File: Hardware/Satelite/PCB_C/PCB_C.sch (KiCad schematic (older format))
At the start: 49 parts, among them IC1 MCP1501T-33E_CHY, J1 SWD, J3 Conector_PCB_B-C, J4 Conector_Expansion_CanSat, J5 USB_B_Micro, M1 Spacer, M2 Spacer, M3 Spacer, U1 TXS0104ERGYR, U2 TCA9802DGKR, U3 W25Q32JVSSIQ, U4 TXS0104ERGYR, U5 BL654, Y1 LFXTAL016178

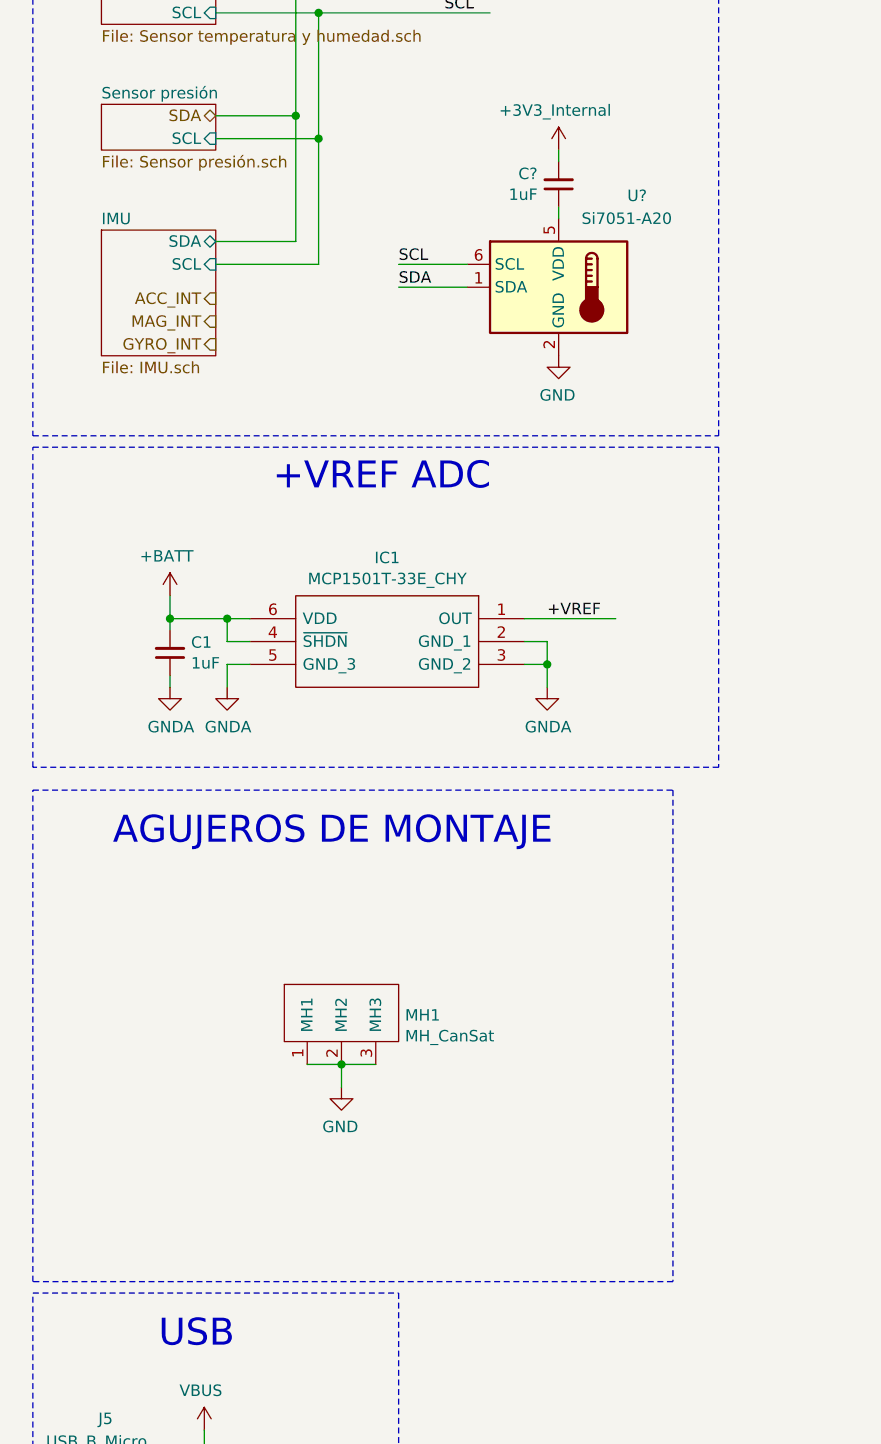
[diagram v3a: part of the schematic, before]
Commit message: Eliminada referencia de tensión no usada en PCB_C
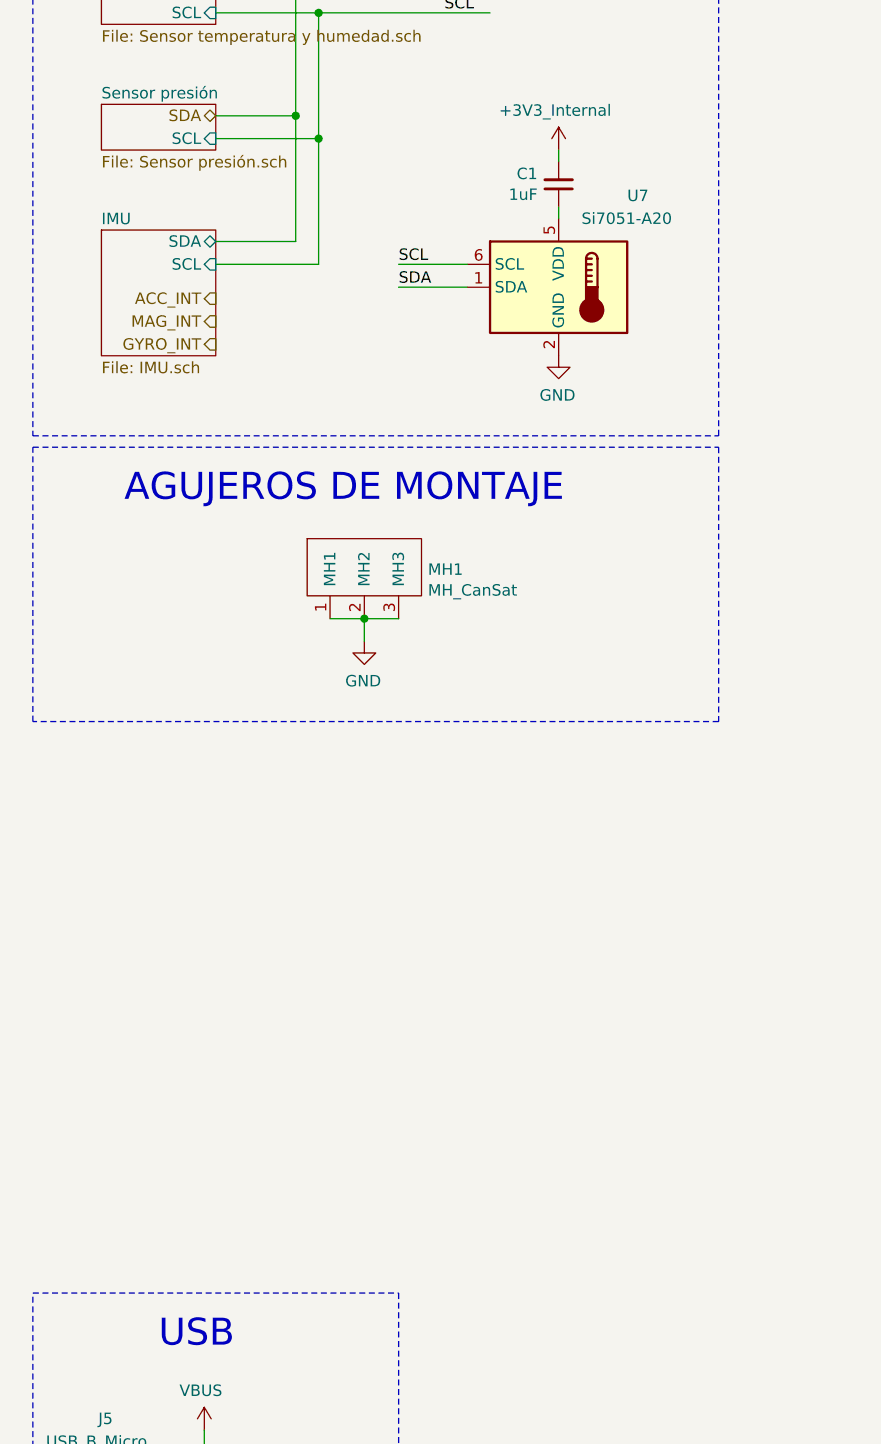
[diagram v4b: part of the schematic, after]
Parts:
- removed C1: 1uF, Capacitor_SMD:C_0402_1005Metric, symbol Device:C_Small
- removed IC1: MCP1501T-33E_CHY, SamacSys_Parts:SOT95P270X145-6N, symbol SamacSys_Parts:MCP1501T-33E_CHY
- gave numbers to parts that had none: 2
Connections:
- net labels removed: GNDA
- wire segments 313 -> 299
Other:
- note removed: "+VREF ADC"
- moved on the sheet: MH1
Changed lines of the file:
@@
-$Comp
-L Device:C_Small C?
-U 1 1 5BCA2C7F
-P 1150 4000
-AR Path="/5BB122CA/5BCA2C7F" Ref="C?"  Part="1"
-AR Path="/5BB12371/5BCA2C7F" Ref="C?"  Part="1"
-AR Path="/5BCA2C7F" Ref="C1"  Part="1"
-F 0 "C1" H 1058 3954 50  0000 R CNN
-F 1 "1uF" H 1058 4045 50  0000 R CNN
-F 2 "Capacitor_SMD:C_0402_1005Metric" H 1150 4000 50  0001 C CNN
-F 3 "~" H 1150 4000 50  0001 C CNN
-F 4 "GRM155R61E105KA12D" H 1150 4000 50  0001 C CNN "Manufacturer Part Number"
-	1    1150 4000
-	-1   0    0    1
-$EndComp
 $Comp
 L Device:C_Small C?
@@
 Text Label 10250 5050 2    50   ~ 0
 SPI_BUFFER_EN
-Text Notes 1600 3300 0    118  ~ 0
-+VREF ADC
-Wire Notes Line
-	550  4500 550  3100
-Wire Notes Line
-	3550 4500 550  4500
-Wire Notes Line
-	3550 3100 3550 4500
-Wire Notes Line
-	550  3100 3550 3100
-Wire Wire Line
-	2700 3850 3100 3850
-Text Label 2800 3850 0    50   ~ 0
-+VREF
-Wire Wire Line
-	2800 4050 2800 4150
-Wire Wire Line
-	2700 4050 2800 4050
-Wire Wire Line
-	2800 3950 2700 3950
-Connection ~ 2800 4050
-Wire Wire Line
-	2800 3950 2800 4050
-Wire Wire Line
-	1400 4050 1400 4150
-Wire Wire Line
-	1500 4050 1400 4050
-Wire Wire Line
-	1400 3850 1150 3850
-Wire Wire Line
-	1400 3950 1400 3850
-Wire Wire Line
-	1500 3950 1400 3950
-Connection ~ 1400 3850
-Wire Wire Line
-	1500 3850 1400 3850
-Wire Wire Line
-	1150 4100 1150 4150
-Wire Wire Line
-	1150 3900 1150 3850
-Connection ~ 1150 3850
-Wire Wire Line
-	1150 3850 1150 3750
-$Comp
-L SamacSys_Parts:MCP1501T-33E_CHY IC1
-U 1 1 5BC3E089
-P 2700 3850
-F 0 "IC1" H 3300 4116 50  0000 C CNN
-F 1 "MCP1501T-33E_CHY" H 3300 4024 50  0000 C CNN
-F 2 "SamacSys_Parts:SOT95P270X145-6N" H 3750 3950 50  0001 L CNN
-F 3 "https://componentsearchengine.com/Datasheets/1/MCP1501T-33E_CHY.pdf" H 3750 3850 50  0001 L CNN
-F 4 "Voltage References Precision Buffered Voltage Reference" H 3750 3750 50  0001 L CNN "Description"
-F 5 "1.45" H 3750 3650 50  0001 L CNN "Height"
-F 6 "Microchip" H 3750 3550 50  0001 L CNN "Manufacturer_Name"
-F 7 "MCP1501T-33E/CHY" H 3750 3450 50  0001 L CNN "Manufacturer Part Number"
-F 8 "MCP1501T-33E/CHY" H 3750 3150 50  0001 L CNN "Arrow Part Number"
-F 9 "https://www.arrow.com/en/products/mcp1501t-33echy/microchip-technology" H 3750 3050 50  0001 L CNN "Arrow Price/Stock"
-	1    2700 3850
-	-1   0    0    -1
-$EndComp
 $Comp
 L AXTEC_IC:Conector_Expansion_CanSat J4
@@
 Wire Wire Line
 	15100 4650 15550 4650
-$Comp
-L power:+BATT #PWR01
-U 1 1 5BC3E6F0
-P 1150 3750
-F 0 "#PWR01" H 1150 3600 50  0001 C CNN
-F 1 "+BATT" H 1165 3923 50  0000 C CNN
-F 2 "" H 1150 3750 50  0001 C CNN
-F 3 "" H 1150 3750 50  0001 C CNN
-	1    1150 3750
-	-1   0    0    -1
-$EndComp
 $Comp
 L Graphic:Logo_Open_Hardware_Large #LOGO1
@@
 Wire Wire Line
 	13500 8750 13850 8750
-$Comp
-L power:GNDA #PWR0103
-U 1 1 5C301DAD
-P 2800 4150
-F 0 "#PWR0103" H 2800 3900 50  0001 C CNN
-F 1 "GNDA" H 2804 3976 50  0000 C CNN
-F 2 "" H 2800 4150 50  0001 C CNN
-F 3 "" H 2800 4150 50  0001 C CNN
-	1    2800 4150
-	1    0    0    -1
-$EndComp
-$Comp
-L power:GNDA #PWR0106
-U 1 1 5C375184
-P 1400 4150
-F 0 "#PWR0106" H 1400 3900 50  0001 C CNN
-F 1 "GNDA" H 1404 3976 50  0000 C CNN
-F 2 "" H 1400 4150 50  0001 C CNN
-F 3 "" H 1400 4150 50  0001 C CNN
-	1    1400 4150
-	1    0    0    -1
-$EndComp
-$Comp
-L power:GNDA #PWR0107
-U 1 1 5C375315
-P 1150 4150
-F 0 "#PWR0107" H 1150 3900 50  0001 C CNN
-F 1 "GNDA" H 1154 3976 50  0000 C CNN
-F 2 "" H 1150 4150 50  0001 C CNN
-F 3 "" H 1150 4150 50  0001 C CNN
-	1    1150 4150
-	1    0    0    -1
-$EndComp
 $Bitmap
 Pos 12950 10250
@@
 	2600 11150 5650 11150
 Wire Notes Line
-	550  6750 550  4600
+	550  4300 550  3100
 Wire Notes Line
-	3350 6750 550  6750
-Wire Notes Line
-	3350 4600 3350 6750
-Wire Notes Line
-	550  4600 3350 4600
+	550  3100 3550 3100
 $Comp
 L Device:R R6
@@
 	1    0    0    -1
 $EndComp
-$Comp
-L AXTEC_IC:MH_CanSat MH1
-U 1 1 5BCAAD71
-P 1900 5700
-F 0 "MH1" H 2178 5815 50  0000 L CNN
-F 1 "MH_CanSat" H 2178 5724 50  0000 L CNN
-F 2 "AXTEC:MH_CanSat" H 1900 5700 50  0001 C CNN
-F 3 "" H 1900 5700 50  0001 C CNN
-	1    1900 5700
-	1    0    0    -1
-$EndComp
-$Comp
-L power:GND #PWR081
-U 1 1 5BCAAE9A
-P 1900 5900
-F 0 "#PWR081" H 1900 5650 50  0001 C CNN
-F 1 "GND" H 1905 5727 50  0000 C CNN
-F 2 "" H 1900 5900 50  0001 C CNN
-F 3 "" H 1900 5900 50  0001 C CNN
-	1    1900 5900
-	-1   0    0    -1
-$EndComp
-Wire Wire Line
-	1750 5800 1900 5800
-Connection ~ 1900 5800
-Wire Wire Line
-	1900 5800 2050 5800
-Wire Wire Line
-	1900 5900 1900 5800
-Text Notes 900  4850 0    118  ~ 0
+Text Notes 950  3350 0    118  ~ 0
 AGUJEROS DE MONTAJE
 Wire Wire Line
@@
 nRST
 $Comp
-L Sensor_Temperature:Si7051-A20 U?
+L Sensor_Temperature:Si7051-A20 U7
 U 1 1 5D3B31C1
 P 2850 2400
-F 0 "U?" H 3150 2800 50  0000 L CNN
+F 0 "U7" H 3150 2800 50  0000 L CNN
 F 1 "Si7051-A20" H 2950 2700 50  0000 L CNN
 F 2 "Package_DFN_QFN:DFN-6-1EP_3x3mm_P1mm_EP1.65x2.55mm" H 2850 2000 50  0001 C CNN
@@
 $EndComp
 $Comp
-L AXTEC_IC:+3V3_Internal #PWR?
+L AXTEC_IC:+3V3_Internal #PWR1
 U 1 1 5D3FBC3E
 P 2850 1800
-F 0 "#PWR?" H 2850 2200 50  0001 C CNN
+F 0 "#PWR1" H 2850 2200 50  0001 C CNN
 F 1 "+3V3_Internal" H 2835 1973 50  0000 C CNN
 F 2 "" H 2850 1800 50  0001 C CNN
@@
 AR Path="/5BB122CA/5D3FD0BC" Ref="C?"  Part="1"
 AR Path="/5BB12371/5D3FD0BC" Ref="C?"  Part="1"
-F 0 "C?" H 2758 1904 50  0000 R CNN
+AR Path="/5D3FD0BC" Ref="C1"  Part="1"
+F 0 "C1" H 2758 1904 50  0000 R CNN
 F 1 "1uF" H 2758 1995 50  0000 R CNN
 F 2 "Capacitor_SMD:C_0402_1005Metric" H 2850 1950 50  0001 C CNN
@@
 	2850 2050 2850 2100
 $Comp
-L power:GND #PWR?
+L power:GND #PWR041
 U 1 1 5D45F3A9
 P 2850 2700
-F 0 "#PWR?" H 2850 2450 50  0001 C CNN
+F 0 "#PWR041" H 2850 2450 50  0001 C CNN
 F 1 "GND" H 2855 2527 50  0000 C CNN
 F 2 "" H 2850 2700 50  0001 C CNN
@@
 Text Label 2150 2300 0    50   ~ 0
 SCL
+Wire Notes Line
+	3550 3100 3550 4300
+Wire Notes Line
+	3550 4300 550  4300
+Wire Wire Line
+	2000 3950 2000 3850
+Wire Wire Line
+	2000 3850 2150 3850
+Connection ~ 2000 3850
+Wire Wire Line
+	1850 3850 2000 3850
+$Comp
+L power:GND #PWR081
+U 1 1 5BCAAE9A
+P 2000 3950
+F 0 "#PWR081" H 2000 3700 50  0001 C CNN
+F 1 "GND" H 2005 3777 50  0000 C CNN
+F 2 "" H 2000 3950 50  0001 C CNN
+F 3 "" H 2000 3950 50  0001 C CNN
+	1    2000 3950
+	-1   0    0    -1
+$EndComp
+$Comp
+L AXTEC_IC:MH_CanSat MH1
+U 1 1 5BCAAD71
+P 2000 3750
+F 0 "MH1" H 2278 3865 50  0000 L CNN
+F 1 "MH_CanSat" H 2278 3774 50  0000 L CNN
+F 2 "AXTEC:MH_CanSat" H 2000 3750 50  0001 C CNN
+F 3 "" H 2000 3750 50  0001 C CNN
+	1    2000 3750
+	1    0    0    -1
+$EndComp
 $EndSCHEMATC

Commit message: Agregado footprints faltantes en PCB_C
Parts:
- U1, U4: footprint RGY(S-PVQFN-N14) -> Package_DFN_QFN:Texas_S-PVQFN-N14
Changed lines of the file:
@@
 F 0 "U4" H 10150 10365 50  0000 C CNN
 F 1 "TXS0104ERGYR" H 10150 10274 50  0000 C CNN
-F 2 "RGY(S-PVQFN-N14)" H 10750 10200 50  0001 L CNN
+F 2 "Package_DFN_QFN:Texas_S-PVQFN-N14" H 10750 10200 50  0001 L CNN
 F 3 "http://www.ti.com/general/docs/lit/getliterature.tsp?genericPartNumber=TXS0104E&&fileType=pdf" H 10750 10100 50  0001 L CNN
 F 4 "Texas Instruments TXS0104ERGYR, Voltage Level Translator, Open Drain, 1.65  3.6 V, 2.3  5.5 V, 14-Pin" H 10750 10000 50  0001 L CNN "Description"
@@
 F 0 "U1" H 4100 10365 50  0000 C CNN
 F 1 "TXS0104ERGYR" H 4100 10274 50  0000 C CNN
-F 2 "RGY(S-PVQFN-N14)" H 4700 10200 50  0001 L CNN
+F 2 "Package_DFN_QFN:Texas_S-PVQFN-N14" H 4700 10200 50  0001 L CNN
 F 3 "http://www.ti.com/general/docs/lit/getliterature.tsp?genericPartNumber=TXS0104E&&fileType=pdf" H 4700 10100 50  0001 L CNN
 F 4 "Texas Instruments TXS0104ERGYR, Voltage Level Translator, Open Drain, 1.65  3.6 V, 2.3  5.5 V, 14-Pin" H 4700 10000 50  0001 L CNN "Description"

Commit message: Agregados footprints faltantes en samacsys + asignacion en PCB_C
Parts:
- U7: footprint Package_DFN_QFN:DFN-6-1EP_3x3mm_P1mm_EP1.65x2.55mm -> Package_DFN_QFN:DFN-6-1EP_3x3mm_P1mm_EP1.5x2.4mm
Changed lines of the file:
@@
 F 0 "U7" H 3150 2800 50  0000 L CNN
 F 1 "Si7051-A20" H 2950 2700 50  0000 L CNN
-F 2 "Package_DFN_QFN:DFN-6-1EP_3x3mm_P1mm_EP1.65x2.55mm" H 2850 2000 50  0001 C CNN
+F 2 "Package_DFN_QFN:DFN-6-1EP_3x3mm_P1mm_EP1.5x2.4mm" H 2850 2000 50  0001 C CNN
 F 3 "https://www.silabs.com/documents/public/data-sheets/Si7050-1-3-4-5-A20.pdf" H 2650 2700 50  0001 C CNN
 F 4 "SI7051-A20-IM" H 2850 2400 50  0001 C CNN "Manufacturer Part Number"

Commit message: PCB_C V2 terminado
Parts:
- removed TP15: TestPoint_RXDBG, TestPoint:TestPoint_Pad_D1.0mm, symbol Connector:TestPoint_Probe
- TP1, TP10, TP11, TP2, TP3, TP4, TP7, TP8, TP9: footprint TestPoint:TestPoint_Pad_D1.0mm -> TestPoint:TestPoint_Pad_D1.5mm
- TP12: value TestPoint_SCLPIC -> TestPoint_SD0; footprint TestPoint:TestPoint_Pad_D1.0mm -> TestPoint:TestPoint_Pad_D1.5mm
- TP13: value TestPoint_SDAPIC -> TestPoint_SCLK; footprint TestPoint:TestPoint_Pad_D1.0mm -> TestPoint:TestPoint_Pad_D1.5mm
- TP14: value TestPoint_TXDBG -> TestPoint_CS; footprint TestPoint:TestPoint_Pad_D1.0mm -> TestPoint:TestPoint_Pad_D1.5mm
- TP5: footprint TestPoint:TestPoint_THTPad_1.0x1.0mm_Drill0.5mm -> TestPoint:TestPoint_THTPad_1.5x1.5mm_Drill0.7mm
- TP6: value TestPoint_VREF -> TestPoint_SDI; footprint TestPoint:TestPoint_Pad_D1.0mm -> TestPoint:TestPoint_Pad_D1.5mm
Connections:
- net labels added: ENABLE_3V3, ENABLE_5V
- net labels removed: +VREF, AUX_ENABLE, CHG_DETECT, RX_DEBUG, SCL_PIC16, SDA_PIC16, TX_DEBUG
- wire segments 299 -> 316
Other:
- moved on the sheet: C1, C6, R1, R4

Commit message: Conectores con más altura y nuevos separadores en PCB_C
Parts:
- J3: Manufacturer Part Number 53307-2071 -> 53353-1071; Notes Hecho con dos 53307-2071 y sus dos opuestos 52465-2071 -> Hecho con dos 53353-1071 y sus dos opuestos 52465-2071
- M1, M2, M3: Manufacturer Part Number R30-3011002 -> R30-3010702
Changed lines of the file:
@@
 F 2 "AXTEC:Conector_PCB_B-C_Lado_C" H 14150 2200 50  0001 C CNN
 F 3 "" H 14150 2200 50  0001 C CNN
-F 4 "Hecho con dos 53307-2071 y sus dos opuestos 52465-2071" H 0   -150 50  0001 C CNN "Notes"
-F 5 "53307-2071" H 14250 1450 50  0001 C CNN "Manufacturer Part Number"
+F 4 "Hecho con dos 53353-1071 y sus dos opuestos 52465-2071" H 0   -150 50  0001 C CNN "Notes"
+F 5 "53353-1071" H 14250 1450 50  0001 C CNN "Manufacturer Part Number"
 F 6 "2" H 14250 1450 50  0001 C CNN "Quantity"
 	1    14250 1450
@@
 F 2 "AXTEC:Empty_Footprint" H 14300 7250 50  0001 C CNN
 F 3 "https://www.mouser.com/datasheet/2/181/R30-301-1135805.pdf" H 14400 7350 50  0001 C CNN
-F 4 "R30-3011002" H 14321 6955 50  0001 R CNN "Manufacturer Part Number"
+F 4 "R30-3010702" H 14321 6955 50  0001 R CNN "Manufacturer Part Number"
 	1    14400 7100
 	-1   0    0    -1
@@
 F 2 "AXTEC:Empty_Footprint" H 14900 7250 50  0001 C CNN
 F 3 "https://www.mouser.com/datasheet/2/181/R30-301-1135805.pdf" H 15000 7350 50  0001 C CNN
-F 4 "R30-3011002" H 14921 6955 50  0001 R CNN "Manufacturer Part Number"
+F 4 "R30-3010702" H 14921 6955 50  0001 R CNN "Manufacturer Part Number"
 	1    15000 7100
 	-1   0    0    -1
@@
 F 2 "AXTEC:Empty_Footprint" H 15500 7250 50  0001 C CNN
 F 3 "https://www.mouser.com/datasheet/2/181/R30-301-1135805.pdf" H 15600 7350 50  0001 C CNN
-F 4 "R30-3011002" H 15521 6955 50  0001 R CNN "Manufacturer Part Number"
+F 4 "R30-3010702" H 15521 6955 50  0001 R CNN "Manufacturer Part Number"
 	1    15600 7100
 	-1   0    0    -1
